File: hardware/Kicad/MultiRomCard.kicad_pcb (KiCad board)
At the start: 2 copper layers, 160 x 100 mm, 16 parts, among them P1 VC4000_Cartridge_Bus, U1 Arduino_UNO, U2 74HC595, U3 74HC595, U4 74HC595, U5 6264, U6 74HC245, U7 74HC245, U8 74HC245

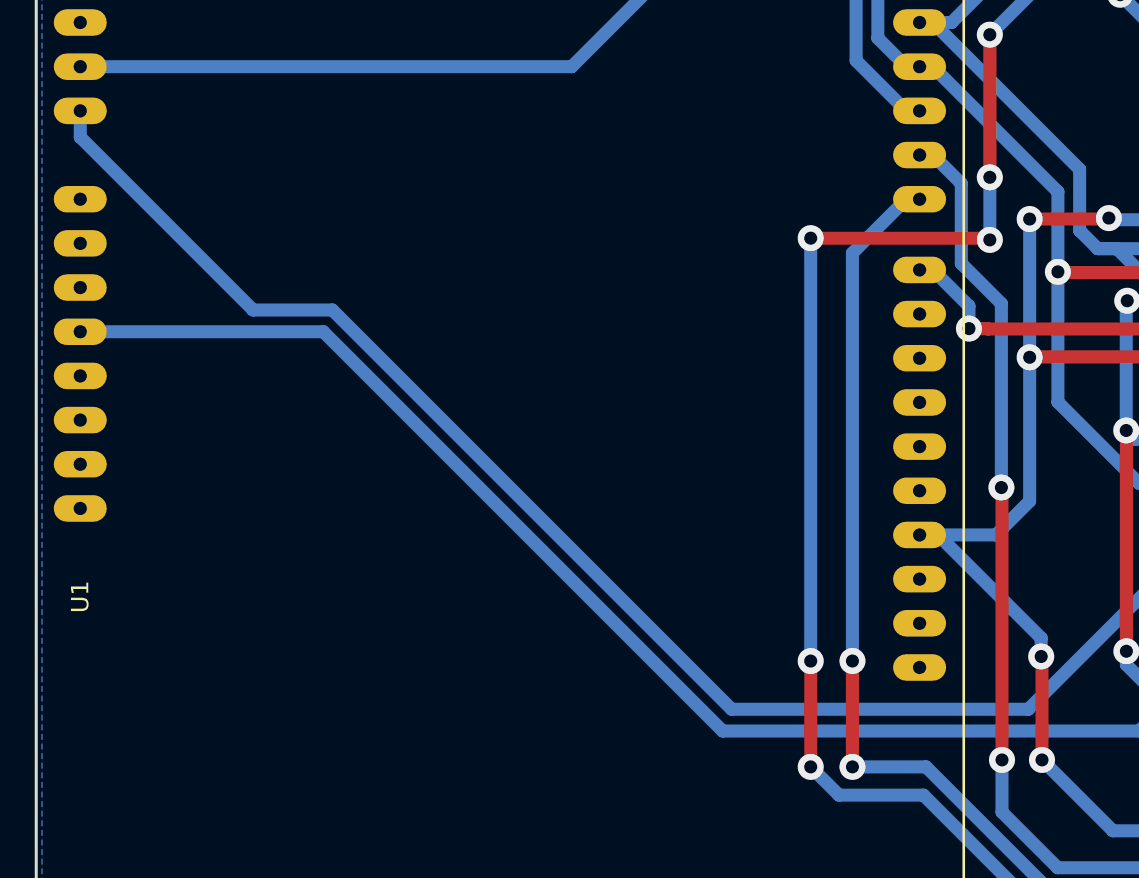
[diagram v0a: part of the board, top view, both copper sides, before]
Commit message: [SCH/PCB] Added and connected missing Arduino GND Pins.
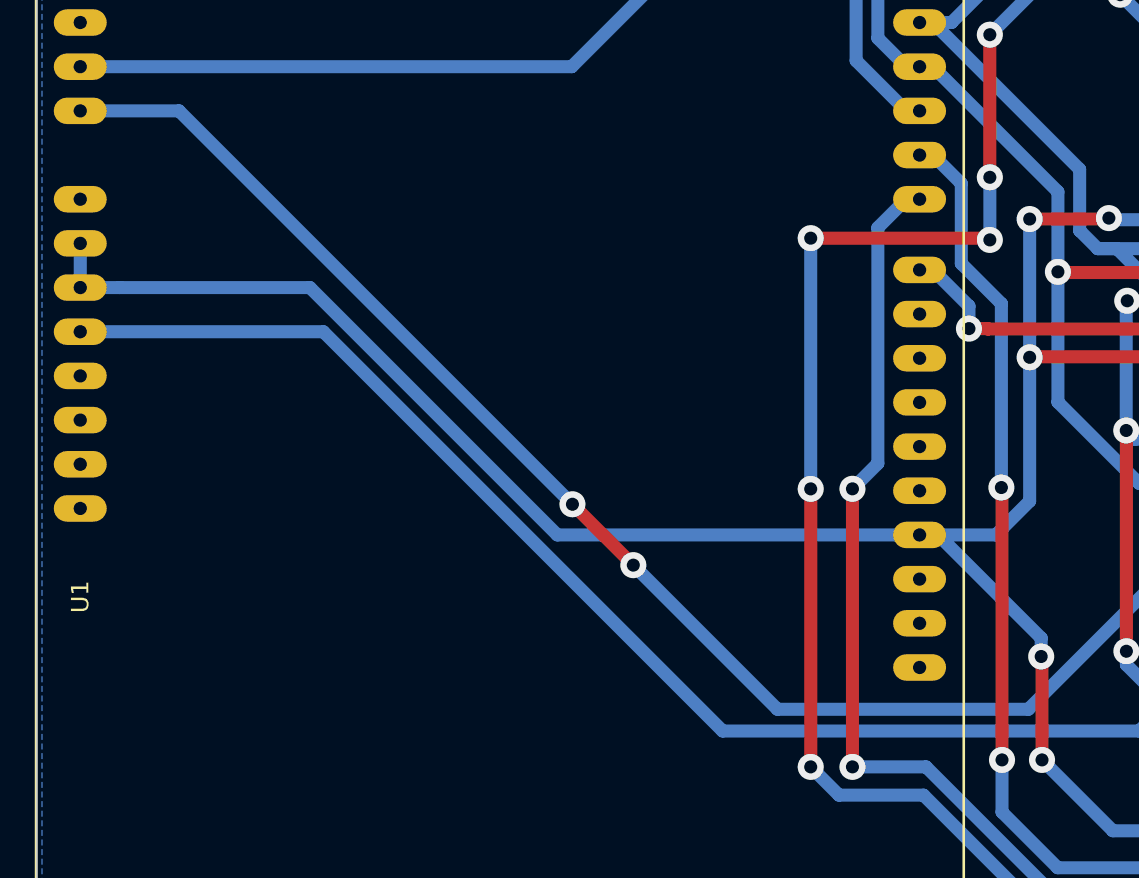
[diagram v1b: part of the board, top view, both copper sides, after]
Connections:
- U1 pad 24: (no net) -> GND
- U1 pad 25: (no net) -> GND
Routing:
- net GND: track 460.1 -> 516.7 mm
- net Net-(U1-Pad27): track 81.2 -> 80.3 mm, vias 0 -> 2
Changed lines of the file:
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@@
 (kicad_pcb (version 4) (host pcbnew "(2015-06-18 BZR 5783)-product")
   (general
-    (links 125)
+    (links 127)
     (no_connects 0)
     (area 64.884999 48.449999 229.051191 155.905001)
     (thickness 1.6)
     (drawings 8)
-    (tracks 853)
+    (tracks 861)
     (zones 0)
     (modules 16)
@@
   (title_block
     (title "Interton VC4000 MultiRom Cartridge")
-    (date "Saturday, June 20, 2015")
+    (date "Sunday, June 21, 2015")
     (rev 0.1)
     (company "Mario Keller and Johannes Maibaum")
@@
     (pad 26 thru_hole oval (at -15.24 25.4 270) (size 1.524 3.048) (drill 0.762) (layers *.Cu *.Mask F.SilkS)
       (net 50 "Net-(U1-Pad26)"))
-    (pad 25 thru_hole oval (at -12.7 25.4 270) (size 1.524 3.048) (drill 0.762) (layers *.Cu *.Mask F.SilkS))
-    (pad 24 thru_hole oval (at -10.16 25.4 270) (size 1.524 3.048) (drill 0.762) (layers *.Cu *.Mask F.SilkS))
+    (pad 25 thru_hole oval (at -12.7 25.4 270) (size 1.524 3.048) (drill 0.762) (layers *.Cu *.Mask F.SilkS)
+      (net 25 GND))
+    (pad 24 thru_hole oval (at -10.16 25.4 270) (size 1.524 3.048) (drill 0.762) (layers *.Cu *.Mask F.SilkS)
+      (net 25 GND))
     (pad 23 thru_hole oval (at -7.62 25.4 270) (size 1.524 3.048) (drill 0.762) (layers *.Cu *.Mask F.SilkS)
       (net 13 VCC))
@@
   (via (at 169 93.9) (size 1.5) (drill 0.75) (layers F.Cu B.Cu) (net 18))
   (via (at 133.102596 82.522741) (size 1.5) (drill 0.75) (layers F.Cu B.Cu) (net 18))
+  (segment (start 110.5 119.415199) (end 110.5 135.4) (width 0.75) (layer F.Cu) (net 19))
+  (segment (start 110.5 119.415199) (end 110.5 105) (width 0.75) (layer B.Cu) (net 19))
   (segment (start 110.5 135.4) (end 112.125001 137.025001) (width 0.75) (layer B.Cu) (net 19))
   (segment (start 112.125001 137.025001) (end 116.98944 137.025001) (width 0.75) (layer B.Cu) (net 19))
@@
   (segment (start 178.82 95.92) (end 179.82 95.92) (width 0.75) (layer B.Cu) (net 19))
   (segment (start 179.82 95.92) (end 182.114998 95.92) (width 0.75) (layer B.Cu) (net 19))
-  (segment (start 110.5 129.315199) (end 110.5 105) (width 0.75) (layer B.Cu) (net 19))
-  (segment (start 110.5 135.4) (end 110.5 129.315199) (width 0.75) (layer F.Cu) (net 19))
   (segment (start 178.5 98.9) (end 178.5 144.3) (width 0.75) (layer F.Cu) (net 19))
   (segment (start 178.5 144.3) (end 178.4 144.4) (width 0.75) (layer F.Cu) (net 19))
@@
   (via (at 120.8 93.3) (size 1.5) (drill 0.75) (layers F.Cu B.Cu) (net 19))
   (via (at 110.5 135.4) (size 1.5) (drill 0.75) (layers F.Cu B.Cu) (net 19))
-  (via (at 110.5 129.315199) (size 1.5) (drill 0.75) (layers F.Cu B.Cu) (net 19))
+  (via (at 110.5 119.415199) (size 1.5) (drill 0.75) (layers F.Cu B.Cu) (net 19))
   (via (at 110.5 105) (size 1.5) (drill 0.75) (layers F.Cu B.Cu) (net 19))
   (segment (start 129.059399 89.374999) (end 124.725001 89.374999) (width 0.75) (layer B.Cu) (net 19))
@@
   (segment (start 138.9 126.72) (end 187.46 126.72) (width 0.75) (layer B.Cu) (net 24) (status 30))
   (segment (start 187.46 126.72) (end 187.7 126.48) (width 0.75) (layer B.Cu) (net 24) (status 30))
+  (segment (start 116.76 122.064) (end 95.93178 122.064) (width 0.75) (layer B.Cu) (net 25))
+  (segment (start 95.93178 122.064) (end 81.70778 107.84) (width 0.75) (layer B.Cu) (net 25))
+  (segment (start 81.70778 107.84) (end 70.774 107.84) (width 0.75) (layer B.Cu) (net 25))
+  (segment (start 70.774 107.84) (end 68.5 107.84) (width 0.75) (layer B.Cu) (net 25))
+  (segment (start 68.5 105.3) (end 68.5 107.84) (width 0.75) (layer B.Cu) (net 25))
   (segment (start 130.733398 53.3) (end 123.800001 60.233397) (width 0.75) (layer B.Cu) (net 25))
   (segment (start 123.800001 60.233397) (end 123.800001 67.100001) (width 0.75) (layer B.Cu) (net 25))
@@
   (segment (start 137.280001 110.225001) (end 137.305002 110.2) (width 0.75) (layer F.Cu) (net 35))
   (segment (start 119.6 110.2) (end 120.66066 110.2) (width 0.75) (layer F.Cu) (net 35))
+  (segment (start 112.9 119.41257) (end 112.9 135.4) (width 0.75) (layer F.Cu) (net 36))
+  (segment (start 112.9 119.41257) (end 114.36099 117.95158) (width 0.75) (layer B.Cu) (net 36))
+  (segment (start 114.36099 117.95158) (end 114.36099 104.39701) (width 0.75) (layer B.Cu) (net 36))
+  (segment (start 114.36099 104.39701) (end 115.998 102.76) (width 0.75) (layer B.Cu) (net 36))
+  (segment (start 115.998 102.76) (end 116.76 102.76) (width 0.75) (layer B.Cu) (net 36))
   (segment (start 176.8 142.825014) (end 125.761425 142.825014) (width 0.75) (layer B.Cu) (net 36))
   (segment (start 112.9 135.4) (end 117.132219 135.4) (width 0.75) (layer B.Cu) (net 36))
   (segment (start 124.557233 142.825014) (end 125.761425 142.825014) (width 0.75) (layer B.Cu) (net 36))
   (segment (start 117.132219 135.4) (end 124.557233 142.825014) (width 0.75) (layer B.Cu) (net 36))
-  (segment (start 112.9 129.31257) (end 112.9 135.4) (width 0.75) (layer F.Cu) (net 36))
-  (segment (start 112.9 105.858) (end 112.9 129.31257) (width 0.75) (layer B.Cu) (net 36))
   (segment (start 176.8656 101) (end 176.8656 142.759414) (width 0.75) (layer F.Cu) (net 36))
   (segment (start 176.8656 142.759414) (end 176.8 142.825014) (width 0.75) (layer F.Cu) (net 36))
@@
   (segment (start 169.01 96.41) (end 167.3 94.7) (width 0.75) (layer B.Cu) (net 36))
   (segment (start 171.92 96.41) (end 169.01 96.41) (width 0.75) (layer B.Cu) (net 36) (status 10))
-  (via (at 112.9 129.31257) (size 1.5) (drill 0.75) (layers F.Cu B.Cu) (net 36))
-  (segment (start 115.998 102.76) (end 112.9 105.858) (width 0.75) (layer B.Cu) (net 36) (status 10))
-  (segment (start 116.76 102.76) (end 115.998 102.76) (width 0.75) (layer B.Cu) (net 36) (status 30))
+  (via (at 112.9 119.41257) (size 1.5) (drill 0.75) (layers F.Cu B.Cu) (net 36))
   (via (at 112.9 135.4) (size 1.5) (drill 0.75) (layers F.Cu B.Cu) (net 36))
   (via (at 176.8656 101) (size 1.5) (drill 0.75) (layers F.Cu B.Cu) (net 36))
@@
   (via (at 125.06528 77.536609) (size 1.5) (drill 0.75) (layers F.Cu B.Cu) (net 48))
   (segment (start 138.9 93.78) (end 138.5444 93.78) (width 0.75) (layer B.Cu) (net 48))
-  (segment (start 68.5 97.68) (end 68.5 99.192) (width 0.75) (layer B.Cu) (net 49))
-  (segment (start 68.5 99.192) (end 78.43799 109.12999) (width 0.75) (layer B.Cu) (net 49))
-  (segment (start 78.43799 109.12999) (end 82.99777 109.12999) (width 0.75) (layer B.Cu) (net 49))
-  (segment (start 82.99777 109.12999) (end 105.95517 132.08739) (width 0.75) (layer B.Cu) (net 49))
-  (segment (start 105.95517 132.08739) (end 123.01701 132.08739) (width 0.75) (layer B.Cu) (net 49))
+  (segment (start 96.8 120.3) (end 74.18 97.68) (width 0.75) (layer B.Cu) (net 49))
+  (segment (start 74.18 97.68) (end 68.5 97.68) (width 0.75) (layer B.Cu) (net 49))
+  (segment (start 100.3 123.8) (end 96.8 120.3) (width 0.75) (layer F.Cu) (net 49))
+  (via (at 96.8 120.3) (size 1.5) (drill 0.75) (layers F.Cu B.Cu) (net 49))
+  (segment (start 123.01701 132.08739) (end 108.58739 132.08739) (width 0.75) (layer B.Cu) (net 49))
+  (segment (start 108.58739 132.08739) (end 100.3 123.8) (width 0.75) (layer B.Cu) (net 49))
+  (via (at 100.3 123.8) (size 1.5) (drill 0.75) (layers F.Cu B.Cu) (net 49))
   (segment (start 123.01701 132.08739) (end 130.9244 124.18) (width 0.75) (layer B.Cu) (net 49))
   (segment (start 130.9244 124.18) (end 131.28 124.18) (width 0.75) (layer B.Cu) (net 49))

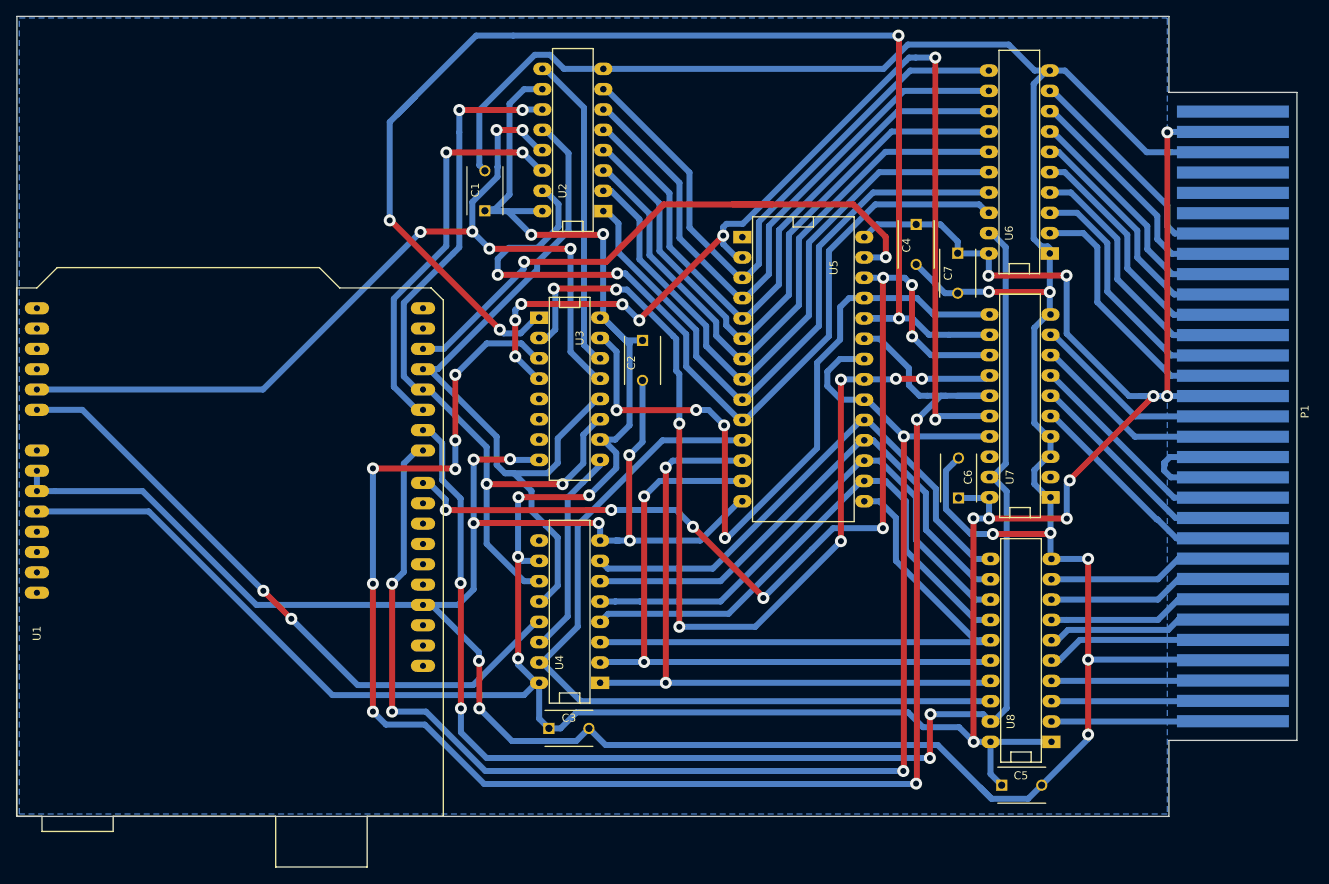
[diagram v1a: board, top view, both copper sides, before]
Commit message: [SCH/PCB] Cleaning up both schematic and PCB a bit.
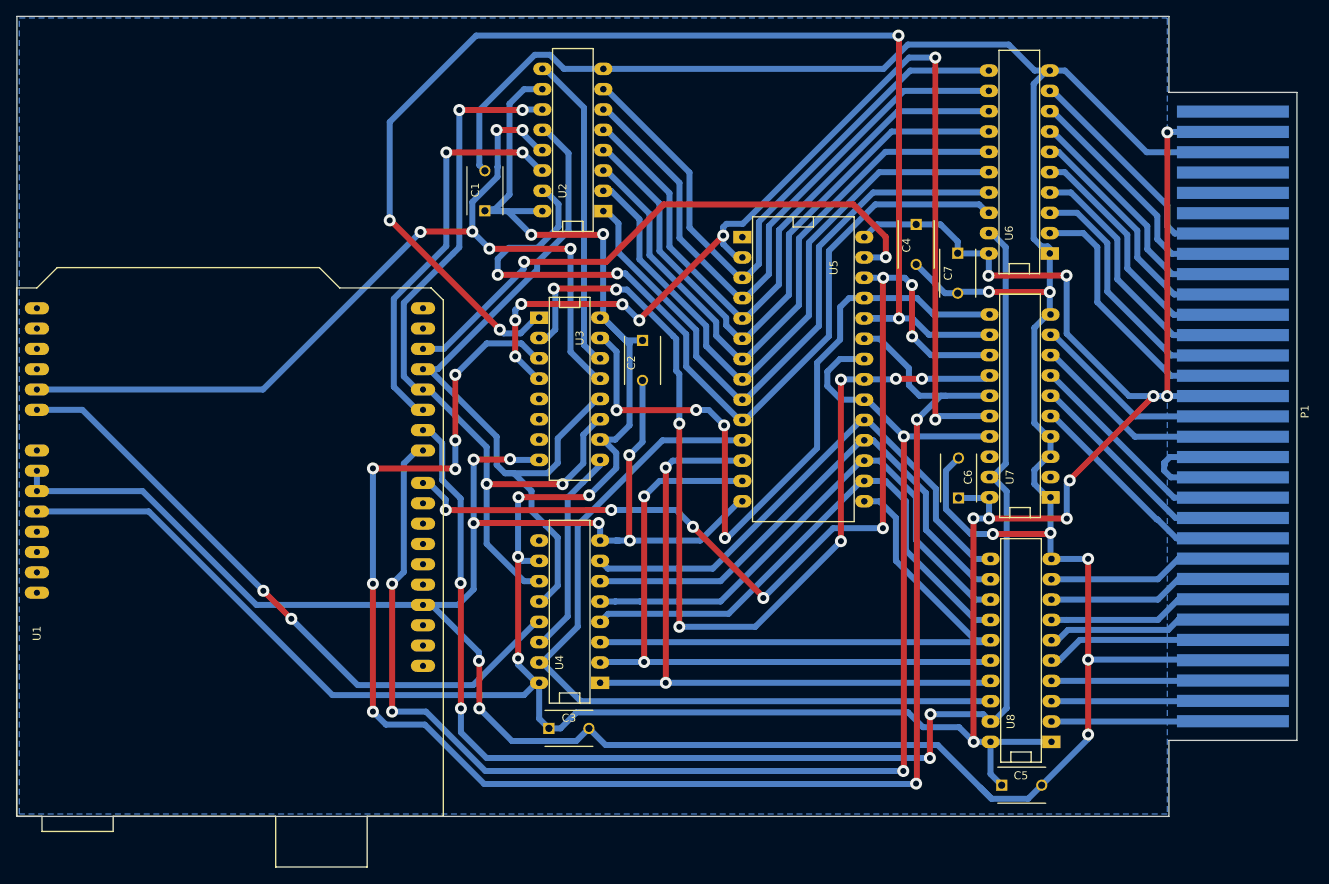
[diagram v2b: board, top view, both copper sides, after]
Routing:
- net WESRAM: track 77.7 -> 72.8 mm
- net /A11: track 211.4 -> 207.3 mm
- net /A9: track 165.1 -> 161.9 mm
- net VCC: track 445.5 -> 443.2 mm
- net /D3: track 76.2 -> 75.0 mm

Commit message: [SCH/PCB] Add Pin header for MicroSD Card Breakout Board.
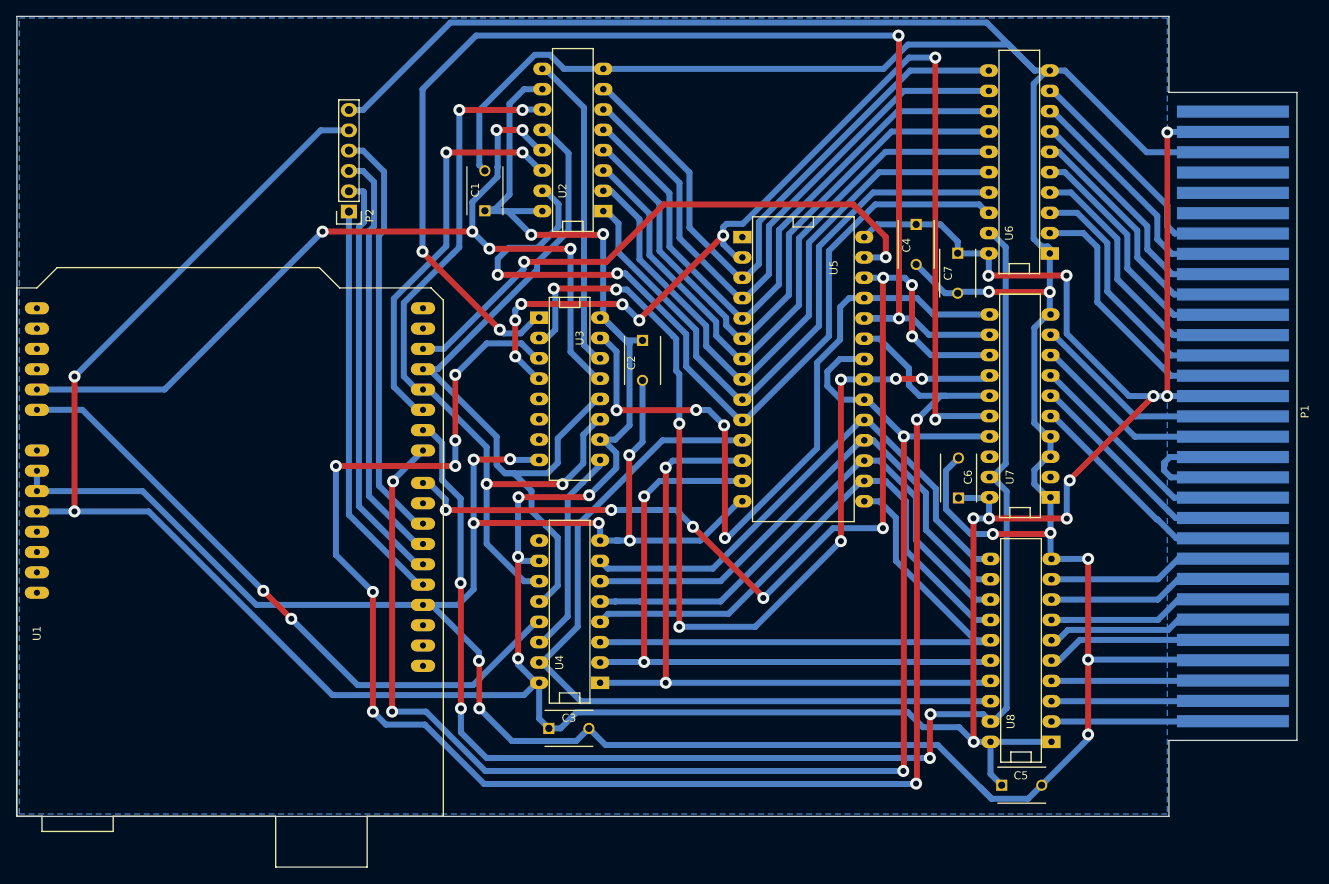
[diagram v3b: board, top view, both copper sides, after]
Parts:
- added P2: MicroSD_Breakout, Pin_Headers:Pin_Header_Straight_1x06, F.Cu at (107.5, 72.9)
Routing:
- net GND: track 516.7 -> 609.5 mm
- net VCC: track 443.2 -> 507.1 mm, vias 16 -> 18
- net Net-(P2-Pad3): track 0.00 -> 52.5 mm
- net Net-(P2-Pad4): track 0.00 -> 52.5 mm
- net Net-(P2-Pad2): track 0.00 -> 52.5 mm
- net Net-(P2-Pad1): track 0.00 -> 50.8 mm
- net /A11: track 207.3 -> 213.7 mm
- net /A9: track 161.9 -> 158.5 mm
